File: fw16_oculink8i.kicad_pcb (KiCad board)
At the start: 4 copper layers, 119 x 73.9 mm, 55 parts, among them J1 Fan, J2 Fan, J3 FXBeam, J4 I2C, J5 USB_A, J6 x8 NPIO, SW1 SW_DPDT_x2, SW2 SW_DIP_x02, U1 BR24G32FVT-3GE2, U2 TL331LV, U3 TL331LV

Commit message: removed all tracks, vias and non position-locked connectors
This is a cleanup before reducing the board size to 10x10cm for cheaper boards.
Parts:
- removed C1, C2, C3, C4, C5: 0.1U, Capacitor_SMD:C_0402_1005Metric
- removed the J4 at (72.1, 82.1)
- removed the J5 at (57.8, 47.5)
- removed R1, R2: 330K, Resistor_SMD:R_0402_1005Metric
- removed R10, R12, R13, R14, R15, R22, R23, R3, R30, R33, R34, R36, R4, R5, R7, R8: 0R, Resistor_SMD:R_0402_1005Metric
- removed R11, R24, R25, R29, R32: 100K, Resistor_SMD:R_0402_1005Metric
- removed R16, R17, R19, R21, R28, R31: 1K, Resistor_SMD:R_0402_1005Metric
- removed R18, R20: 10K, Resistor_SMD:R_0402_1005Metric
- removed R26, R27: 47K, Resistor_SMD:R_0402_1005Metric
- removed R6, R9: 4.7K, Resistor_SMD:R_0402_1005Metric
- removed SW1: SW_DPDT_x2, Switches:SSSS820101
- removed SW2: SW_DIP_x02, Button_Switch_SMD:SW_DIP_SPSTx02_Slide_Copal_CHS-02B_W7.62mm_P1.27mm
- removed U1: BR24G32FVT-3GE2, Package_SO:TSSOP-8_4.4x3mm_P0.65mm
- removed U2, U3: TL331LV, Package_TO_SOT_SMD:SOT-23-5
- J4: renamed from J1; value Fan -> FAN_CON_L
- J5: renamed from J2; value Fan -> FAN_CON_R
- renumbered J3 to J1, J6 to J2
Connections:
- net 12V_FAN renamed +12V
- net 5V_ALW renamed +5V
- J1 pad PA4: 3V3_CTRL -> +3V3
- J1 pad PA5: 3V3_ID -> +3V3
- J1 pad PB4: 3V3_CTRL -> +3V3
- J1 pad PB5: 3V3_ID -> +3V3
- J1 pad PG1: /GPIO0 -> unconnected-(J1A-GPIO0_EC-PadPG1)
- J1 pad PH1: /GPIO1 -> unconnected-(J1A-GPIO1_EC-PadPH1)
- J4 pad 2: /FAN0_SPD -> /FAN0_PWM
- J4 pad 3: /FAN0_PWM -> /FAN0_SPD
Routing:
- net /PERSTA: track 98.7 -> 0.00 mm, vias 2 -> 0
- net /REFCLKB-: track 94.7 -> 0.00 mm, vias 2 -> 0
- net /REFCLKB+: track 94.6 -> 0.00 mm, vias 2 -> 0
- net +12V: track 92.3 -> 0.00 mm, vias 4 -> 0
- net /FAN1_SPD: track 92.0 -> 0.00 mm, vias 4 -> 0
- net /FAN1_PWM: track 89.8 -> 0.00 mm, vias 4 -> 0
- net /CPRSNTA: track 88.9 -> 0.00 mm, vias 2 -> 0
- net /RX1-: track 85.6 -> 0.00 mm
- net /RX1+: track 85.6 -> 0.00 mm
- net /TX3+: track 83.5 -> 0.00 mm, vias 2 -> 0
- net /TX3-: track 83.5 -> 0.00 mm, vias 2 -> 0
- net /TX2-: track 81.1 -> 0.00 mm, vias 2 -> 0
- net /TX2+: track 81.0 -> 0.00 mm, vias 2 -> 0
- net /TX1+: track 80.9 -> 0.00 mm
- net /TX1-: track 80.8 -> 0.00 mm
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- removed copper zone on B.Cu, net +12V
- removed copper zone on F.Cu, net +12V
- removed copper zone on B.Cu, net +5V
- removed copper zone on F.Cu, net +5V
- removed copper zone on B.Cu, net GND
- removed copper zone on F.Cu, net GND
- removed copper zone on In1.Cu, net GND
- removed copper zone on In2.Cu, net GND

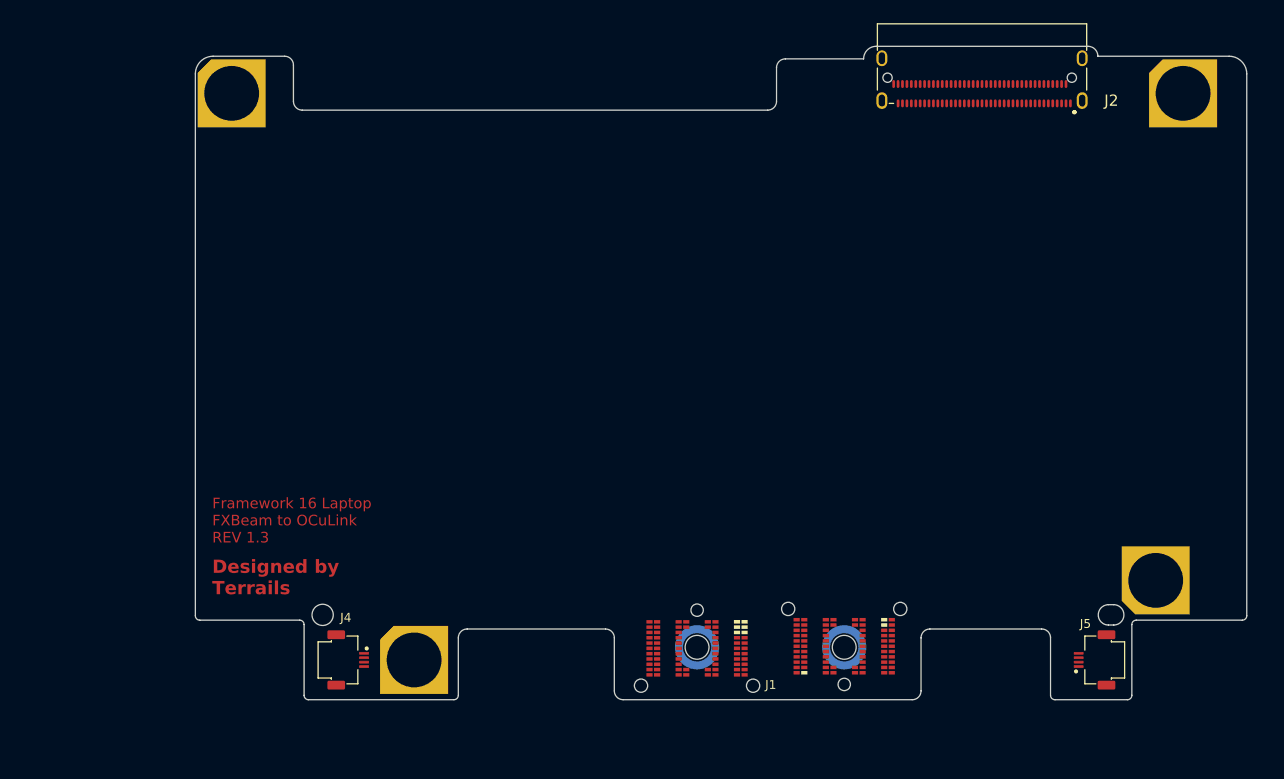
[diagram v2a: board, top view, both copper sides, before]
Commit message: updated PCB shape to be smaller than 10x10cm
All the important things should still be in their right place. The outline is well defined.
One of the mounting hole had to be truncated, may need a small spacer to screw flat.
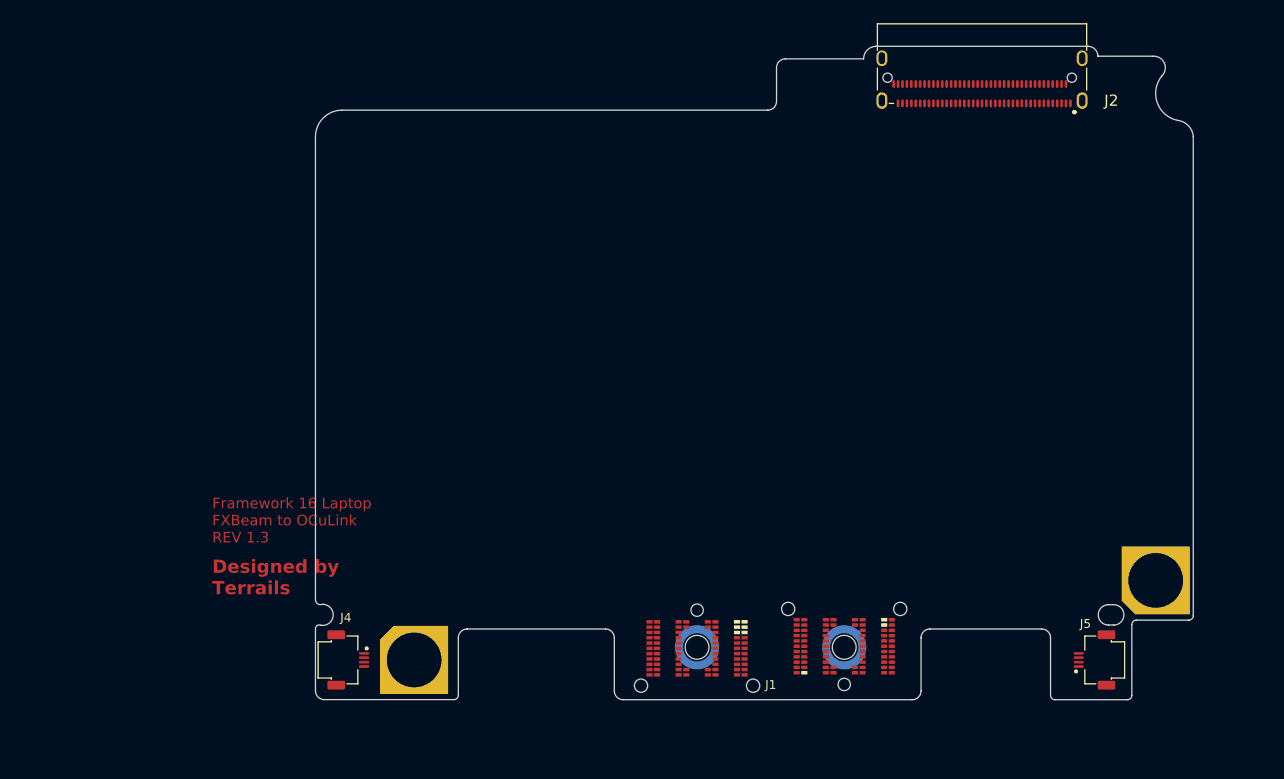
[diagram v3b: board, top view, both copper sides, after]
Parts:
- removed H3, H4: MountingHole_Pad, Expansion_Bay:MountingHole_6.2mm_EasySolder_Cut
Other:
- board size 119 x 73.9 mm -> 99.3 x 73.9 mm

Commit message: routed the boards - passes ERC
Routing done - still need to take care of the silkscreen
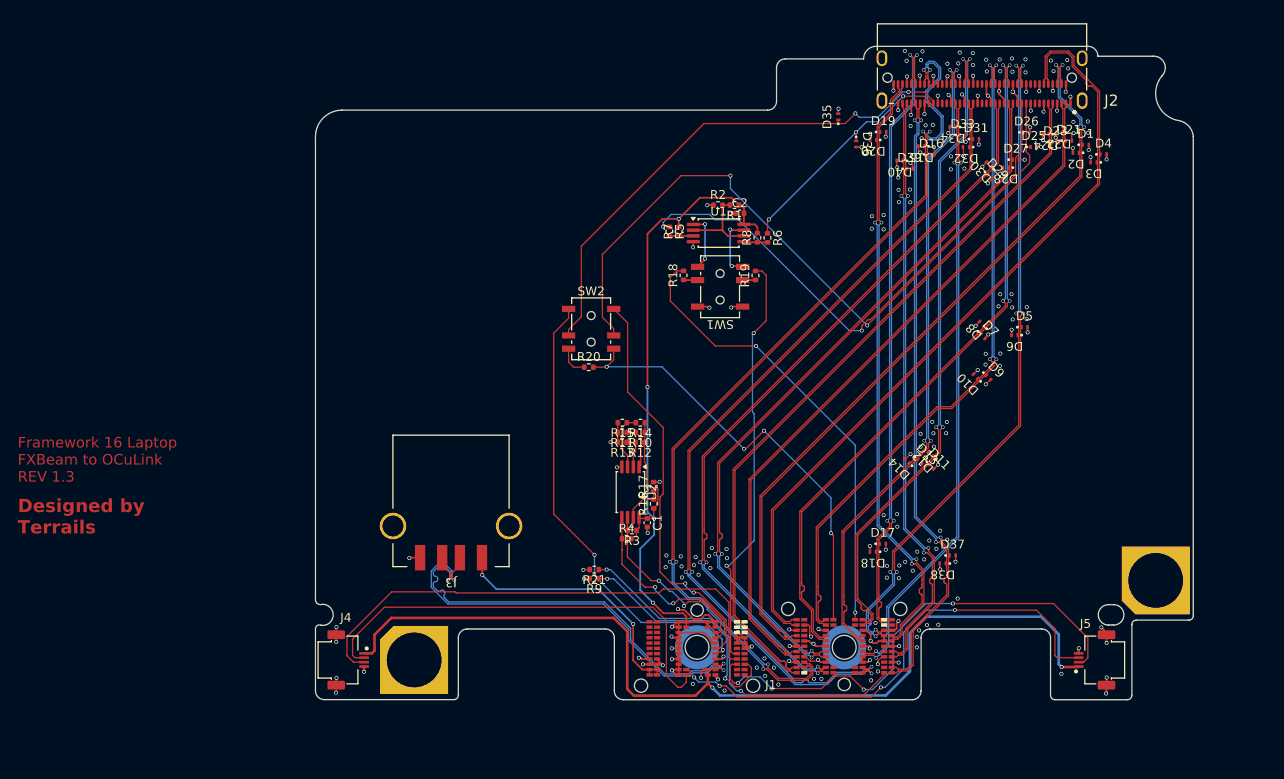
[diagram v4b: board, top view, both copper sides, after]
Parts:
- added C1: 100n, Capacitor_SMD:C_0402_1005Metric, F.Cu at (93.9, 77.1)
- added C2: 100n, Capacitor_SMD:C_0402_1005Metric, F.Cu at (104.4, 42.1)
- added D1: TPD1E01B04, Package_SON:Texas_DPY0002A_0.6x1mm_P0.65mm, F.Cu at (143.5, 34.4)
- added D10: TPD1E01B04, Package_SON:Texas_DPY0002A_0.6x1mm_P0.65mm, F.Cu at (131.1, 60.6)
- added D11: TPD1E01B04, Package_SON:Texas_DPY0002A_0.6x1mm_P0.65mm, F.Cu at (126.1, 70.8)
- added D12: TPD1E01B04, Package_SON:Texas_DPY0002A_0.6x1mm_P0.65mm, F.Cu at (126.0, 69.4)
- added D13: TPD1E01B04, Package_SON:Texas_DPY0002A_0.6x1mm_P0.65mm, F.Cu at (124.7, 70.3)
- added D14: TPD1E01B04, Package_SON:Texas_DPY0002A_0.6x1mm_P0.65mm, F.Cu at (123.3, 70.1)
- added D15: TPD1E01B04, Package_SON:Texas_DPY0002A_0.6x1mm_P0.65mm, F.Cu at (125.0, 34.5)
- added D16: TPD1E01B04, Package_SON:Texas_DPY0002A_0.6x1mm_P0.65mm, F.Cu at (126.1, 35.5)
- added D17: TPD1E01B04, Package_SON:Texas_DPY0002A_0.6x1mm_P0.65mm, F.Cu at (120.6, 79.5)
- added D18: TPD1E01B04, Package_SON:Texas_DPY0002A_0.6x1mm_P0.65mm, F.Cu at (119.5, 80.4)
- added D19: TPD1E01B04, Package_SON:Texas_DPY0002A_0.6x1mm_P0.65mm, F.Cu at (120.6, 32.9)
- added D2: TPD1E01B04, Package_SON:Texas_DPY0002A_0.6x1mm_P0.65mm, F.Cu at (142.4, 35.3)
- added D20: TPD1E01B04, Package_SON:Texas_DPY0002A_0.6x1mm_P0.65mm, F.Cu at (119.5, 33.8)
- added D21: TPD1E01B04, Package_SON:Texas_DPY0002A_0.6x1mm_P0.65mm, F.Cu at (141.6, 33.9)
- added D22: TPD1E01B04, Package_SON:Texas_DPY0002A_0.6x1mm_P0.65mm, F.Cu at (140.5, 33.0)
- added D23: TPD1E01B04, Package_SON:Texas_DPY0002A_0.6x1mm_P0.65mm, F.Cu at (140.1, 34.1)
- added D24: TPD1E01B04, Package_SON:Texas_DPY0002A_0.6x1mm_P0.65mm, F.Cu at (139.0, 33.2)
- added D25: TPD1E01B04, Package_SON:Texas_DPY0002A_0.6x1mm_P0.65mm, F.Cu at (137.6, 34.6)
- added D26: TPD1E01B04, Package_SON:Texas_DPY0002A_0.6x1mm_P0.65mm, F.Cu at (136.8, 33.0)
- added D27: TPD1E01B04, Package_SON:Texas_DPY0002A_0.6x1mm_P0.65mm, F.Cu at (135.6, 36.1)
- added D28: TPD1E01B04, Package_SON:Texas_DPY0002A_0.6x1mm_P0.65mm, F.Cu at (134.5, 37.0)
- added D29: TPD1E01B04, Package_SON:Texas_DPY0002A_0.6x1mm_P0.65mm, F.Cu at (132.7, 38.0)
- added D3: TPD1E01B04, Package_SON:Texas_DPY0002A_0.6x1mm_P0.65mm, F.Cu at (144.4, 36.4)
- added D30: TPD1E01B04, Package_SON:Texas_DPY0002A_0.6x1mm_P0.65mm, F.Cu at (132.5, 36.6)
- added D31: TPD1E01B04, Package_SON:Texas_DPY0002A_0.6x1mm_P0.65mm, F.Cu at (131.1, 33.7)
- added D32: TPD1E01B04, Package_SON:Texas_DPY0002A_0.6x1mm_P0.65mm, F.Cu at (130.0, 34.6)
- added D33: TPD1E01B04, Package_SON:Texas_DPY0002A_0.6x1mm_P0.65mm, F.Cu at (129.6, 33.3)
- added D34: TPD1E01B04, Package_SON:Texas_DPY0002A_0.6x1mm_P0.65mm, F.Cu at (128.5, 32.4)
- added D35: TPD1E01B04, Package_SON:Texas_DPY0002A_0.6x1mm_P0.65mm, F.Cu at (115.5, 31.2)
- added D36: TPD1E01B04, Package_SON:Texas_DPY0002A_0.6x1mm_P0.65mm, F.Cu at (117.6, 34.3)
- added D37: TPD1E01B04, Package_SON:Texas_DPY0002A_0.6x1mm_P0.65mm, F.Cu at (128.5, 80.8)
- added D38: TPD1E01B04, Package_SON:Texas_DPY0002A_0.6x1mm_P0.65mm, F.Cu at (127.4, 81.8)
- added D39: TPD1E01B04, Package_SON:Texas_DPY0002A_0.6x1mm_P0.65mm, F.Cu at (123.6, 37.1)
- added D4: TPD1E01B04, Package_SON:Texas_DPY0002A_0.6x1mm_P0.65mm, F.Cu at (145.5, 35.5)
- added D40: TPD1E01B04, Package_SON:Texas_DPY0002A_0.6x1mm_P0.65mm, F.Cu at (122.5, 36.2)
- added D5: TPD1E01B04, Package_SON:Texas_DPY0002A_0.6x1mm_P0.65mm, F.Cu at (136.6, 55.0)
- added D6: TPD1E01B04, Package_SON:Texas_DPY0002A_0.6x1mm_P0.65mm, F.Cu at (135.5, 55.9)
- added D7: TPD1E01B04, Package_SON:Texas_DPY0002A_0.6x1mm_P0.65mm, F.Cu at (131.9, 56.0)
- added D8: TPD1E01B04, Package_SON:Texas_DPY0002A_0.6x1mm_P0.65mm, F.Cu at (131.8, 54.6)
- added D9: TPD1E01B04, Package_SON:Texas_DPY0002A_0.6x1mm_P0.65mm, F.Cu at (132.5, 60.7)
- added J3: USB_A, USB:87583-2010BLF, F.Cu at (71.7, 77.5)
- added R1: 100K, Resistor_SMD:R_0402_1005Metric, F.Cu at (103.8, 41.2)
- added R10: 0R, Resistor_SMD:R_0402_1005Metric, F.Cu at (93.1, 66.9)
- added R11: 0R, Resistor_SMD:R_0402_1005Metric, F.Cu at (91.1, 66.9)
- added R12: 0R, Resistor_SMD:R_0402_1005Metric, F.Cu at (93.1, 68.0)
- added R13: 0R, Resistor_SMD:R_0402_1005Metric, F.Cu at (91.1, 68.0)
- added R14: 0R, Resistor_SMD:R_0402_1005Metric, F.Cu at (93.2, 65.8)
- added R15: 0R, Resistor_SMD:R_0402_1005Metric, F.Cu at (91.1, 65.8)
- added R16: 100K, Resistor_SMD:R_0402_1005Metric, F.Cu at (94.7, 75.0)
- added R17: 0R, Resistor_SMD:R_0402_1005Metric, F.Cu at (94.7, 73.0)
- added R18: 1K, Resistor_SMD:R_0402_1005Metric, F.Cu at (98.0, 49.1)
- added R19: 1K, Resistor_SMD:R_0402_1005Metric, F.Cu at (106.2, 49.2)
- added R2: 47K, Resistor_SMD:R_0402_1005Metric, F.Cu at (101.9, 41.2)
- added R20: 0R, Resistor_SMD:R_0402_1005Metric, F.Cu at (87.3, 59.5)
- added R21: 330K, Resistor_SMD:R_0402_1005Metric, F.Cu at (87.9, 82.4)
- added R3: 4k7, Resistor_SMD:R_0402_1005Metric, F.Cu at (92.2, 78.0)
- added R4: 4k7, Resistor_SMD:R_0402_1005Metric, F.Cu at (91.6, 78.9)
- added R5: 1K, Resistor_SMD:R_0402_1005Metric, F.Cu at (96.4, 44.2)
- added R6: 1K, Resistor_SMD:R_0402_1005Metric, F.Cu at (107.5, 44.9)
- added R7: 100K, Resistor_SMD:R_0402_1005Metric, F.Cu at (97.5, 44.2)
- added R8: 100K, Resistor_SMD:R_0402_1005Metric, F.Cu at (106.4, 44.9)
- added R9: 330K, Resistor_SMD:R_0402_1005Metric, F.Cu at (87.9, 83.5)
- added SW1: SW_DPDT_x2, Switches:SSSS820101, F.Cu at (102.2, 50.4)
- added SW2: SW_DPDT_x2, Switches:SSSS820101, F.Cu at (87.6, 55.2)
- added U1: LM393, Package_SO:TSSOP-8_4.4x3mm_P0.65mm, F.Cu at (102.0, 44.4)
- added U2: BR24G32FVT-3GE2, Package_SO:TSSOP-8_4.4x3mm_P0.65mm, F.Cu at (92.0, 73.7)
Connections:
- J1 pad SD6: /RX2- -> /RX2+
- J1 pad SE6: /RX2+ -> /RX2-
- J1 pad SK3: /TX4+ -> /TX4-
- J1 pad SL3: /TX4- -> /TX4+
- J2 pad A32: /REFCLKB- -> /REFCLKB+
- J2 pad A33: /REFCLKB+ -> /REFCLKB-
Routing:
- net GND: track 0.00 -> 133.0 mm, vias 0 -> 221
- net +12V: track 0.00 -> 103.7 mm, vias 0 -> 2
- net /REFCLKB-: track 0.00 -> 103.0 mm, vias 0 -> 4
- net /REFCLKB+: track 0.00 -> 100.5 mm, vias 0 -> 4
- net /TX4+: track 0.00 -> 94.9 mm, vias 0 -> 2
- net /TX4-: track 0.00 -> 94.9 mm, vias 0 -> 2
- net +3V3: track 0.00 -> 89.5 mm, vias 0 -> 4
- net /RX1-: track 0.00 -> 89.3 mm
- net /RX1+: track 0.00 -> 89.3 mm
- net /RX0+: track 0.00 -> 86.2 mm, vias 0 -> 2
- net /RX0-: track 0.00 -> 86.2 mm, vias 0 -> 2
- net /TX3+: track 0.00 -> 85.8 mm, vias 0 -> 2
- net /TX3-: track 0.00 -> 85.8 mm, vias 0 -> 2
- net /PERSTA: track 0.00 -> 84.6 mm, vias 0 -> 2
- net /TX2-: track 0.00 -> 83.1 mm, vias 0 -> 2
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- added copper zone on In1.Cu, net GND
- added copper zone on In2.Cu, net GND

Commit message: placement of components Silkscreen done
There is no error left in the ERC (other that two hole clearance violations to ignore)
and the warnings dont matter.
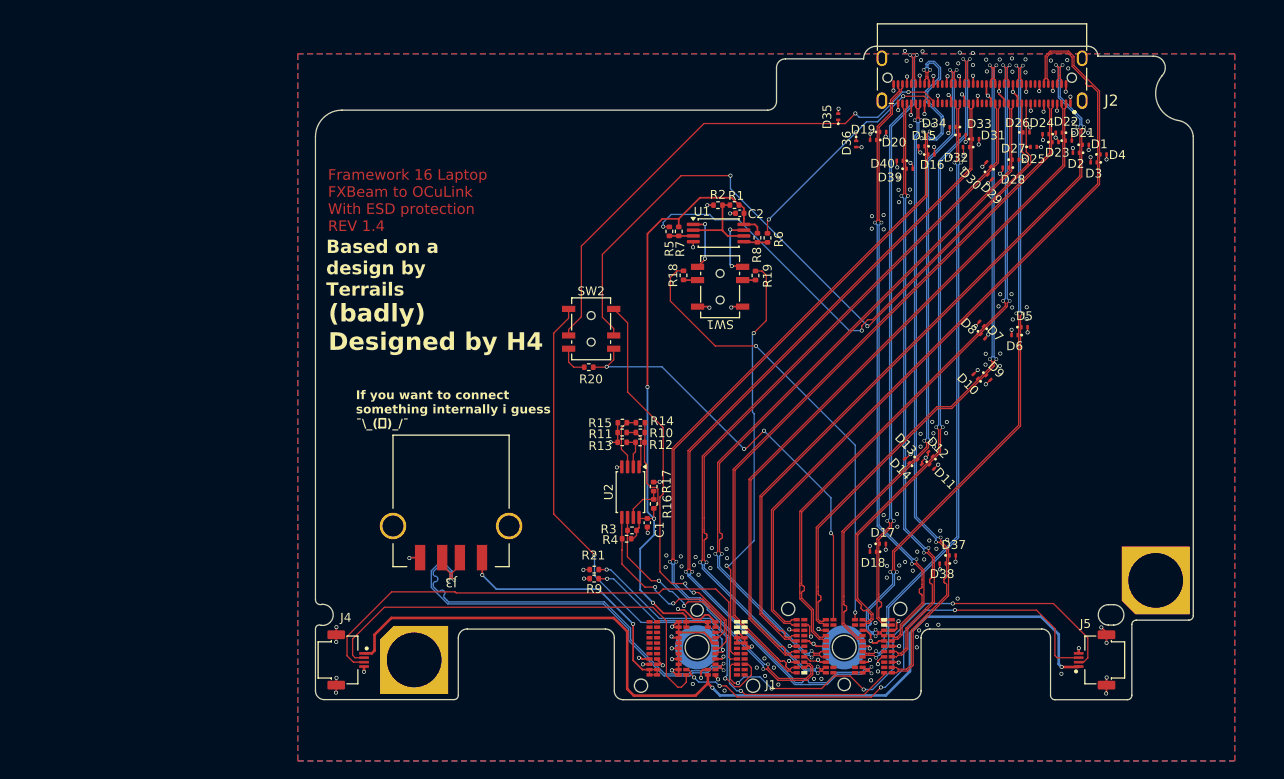
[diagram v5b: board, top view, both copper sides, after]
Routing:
- net /CPRSNTA: track 62.9 -> 63.6 mm
- net GND: vias 221 -> 218
- net +3V3: vias 4 -> 3
- added copper zone on B.Cu, net GND
- added copper zone on F.Cu, net GND
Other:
- board text added: "(badly) Designed by H4"
- board text added: "Based on a design by Terrails"
- board text added: "Framework 16 Laptop FXBeam to OCuLink With ESD protection REV 1.4"
- board text added: "If you want to connect something internally i guess ¯\_(ツ)_/¯"
- board text removed: "Designed by Terrails"
- board text removed: "Framework 16 Laptop FXBeam to OCuLink REV 1.3"

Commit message: added random silkscreen images
because i'm paying for silkscreen so i'm using it!
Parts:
- added G***: LOGO, cat_outline, B.Cu at (82.2, 78.8)
- added G***: LOGO, LOGO, B.Cu at (126.8, 64.7)
- added REF**: Symbol_ESD-Logo_CopperTop, Symbol:Symbol_ESD-Logo_CopperTop, F.Cu at (148.8, 63.3)
- added REF**: OSHW-Logo2_36.5x30mm_SilkScreen, Symbol:OSHW-Logo2_36.5x30mm_SilkScreen, B.Cu at (141.0, 41.8)
